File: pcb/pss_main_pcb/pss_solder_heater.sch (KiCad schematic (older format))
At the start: 43 parts

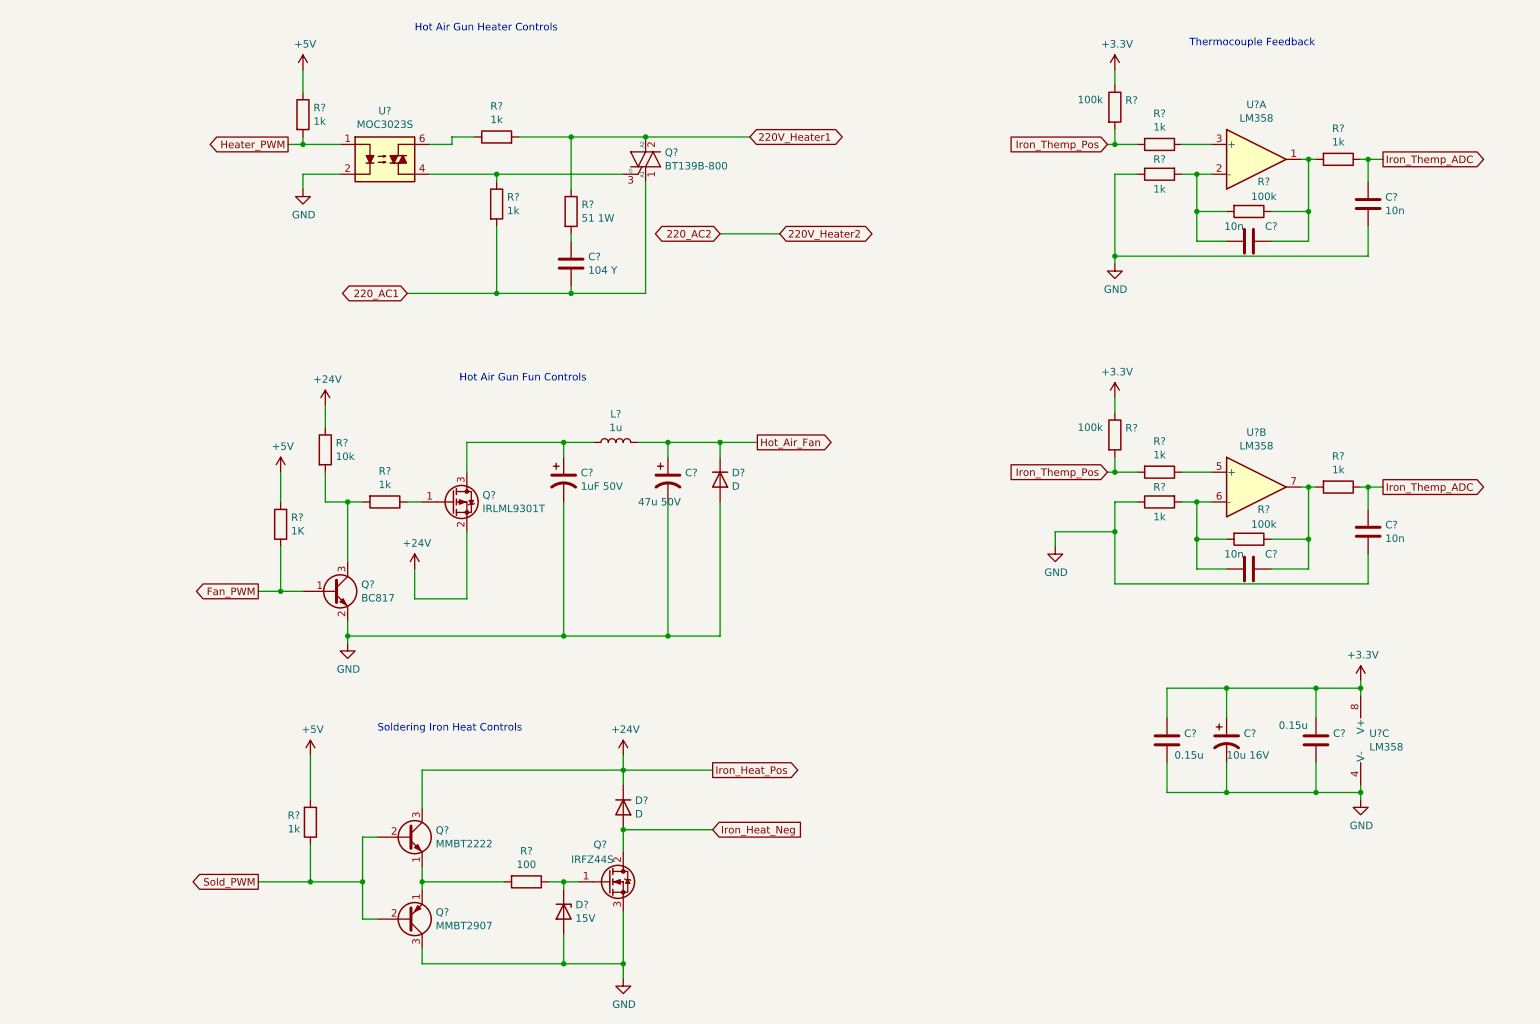
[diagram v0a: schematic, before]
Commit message: Add stm32 schematics
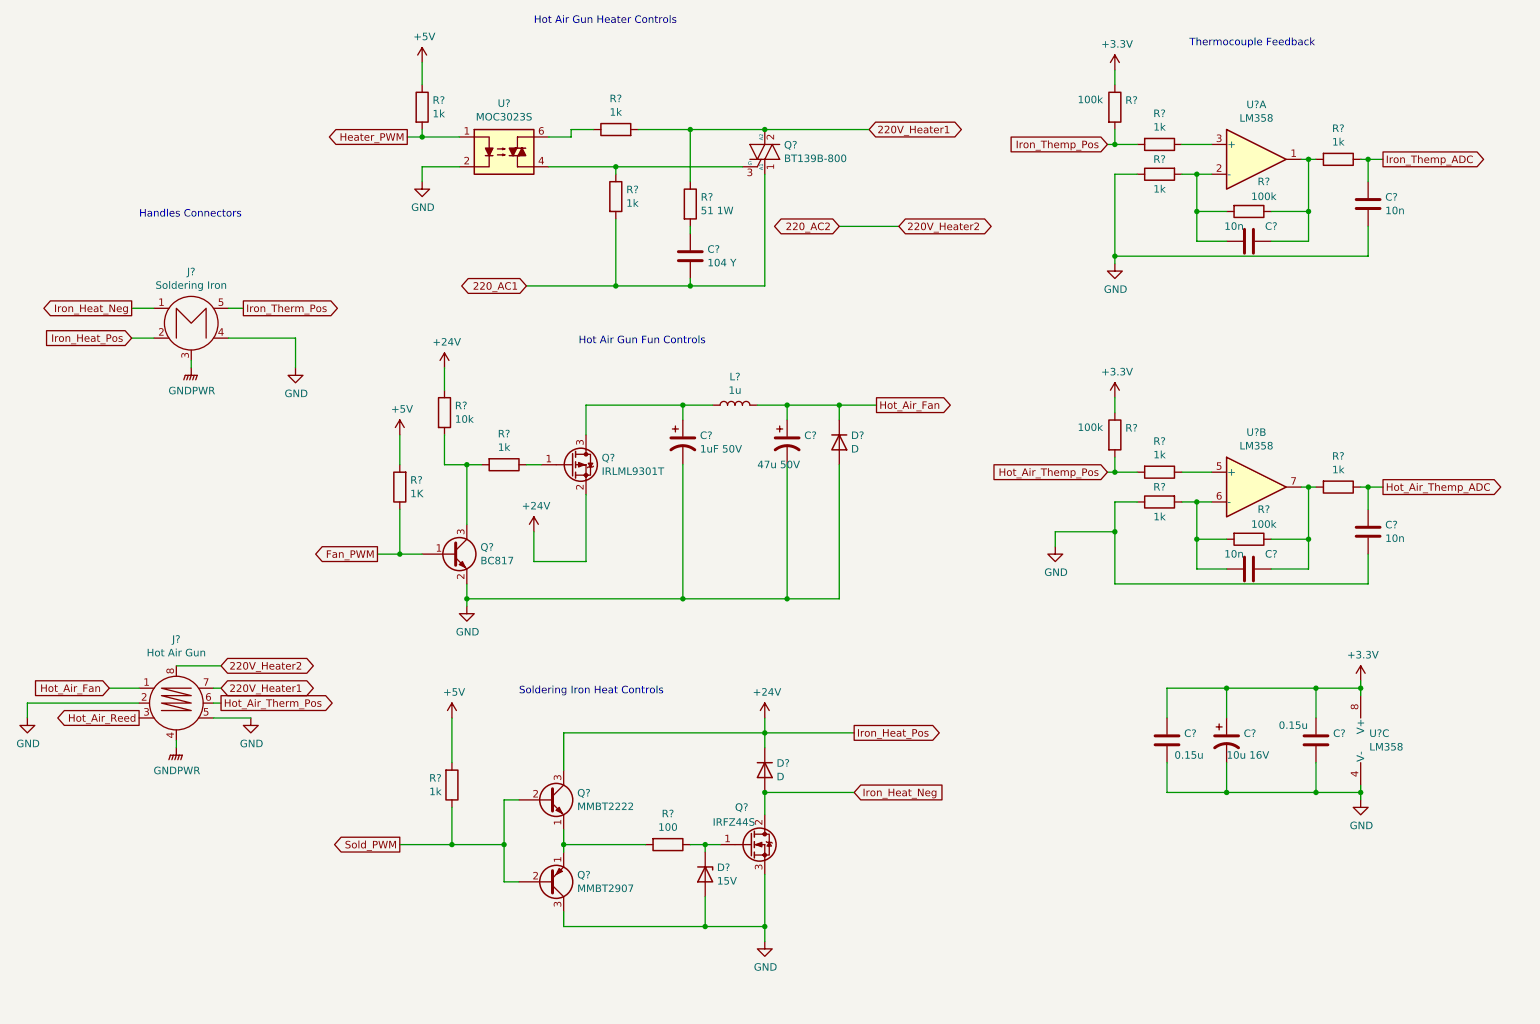
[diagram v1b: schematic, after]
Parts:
- added J?: Soldering Iron, symbol gx16_conn:GX16-M5_connector
- added J?: Hot Air Gun, symbol gx16_conn:GX16-M8_connector
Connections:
- net +24V: now also J?.2
- net 220V_Heater1: now also J?.7
- net 220V_Heater2: now also J?.8
- net GND: now also J?.2, J?.4, J?.5
- net Hot_Air_Fan: now also J?.1
- net Iron_Heat_Neg: now also J?.1
- net Iron_Themp_ADC: no longer C?.1, R?.1
- net Iron_Themp_Pos: no longer R?.2, R?.2
- new net GNDPWR: J?.3, J?.4
- new net Hot_Air_Reed: J?.3
- new net Hot_Air_Themp_ADC: C?.1, R?.1
- new net Hot_Air_Themp_Pos: R?.2, R?.2
- new net Hot_Air_Therm_Pos: J?.6
- new net Iron_Therm_Pos: J?.5
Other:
- note added: "Handles Connectors\n"
- moved on the sheet: C?, D?, L?, Q?, R?, U?

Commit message: Fix schematics
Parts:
- gave numbers to parts that had none: 43
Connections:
- net Hot_Air_Themp_Pos is gone; now on net Hot_Air_Therm_Pos: R12.2, R15.2
- net Iron_Themp_Pos is gone; now on net Iron_Therm_Pos: R11.2, R13.2

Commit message: Add footprints for AC controls components
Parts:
- J3: footprint (none) -> gx_connectors:GX16-8
- U3: footprint (none) -> moc3023s:SOT254P1016X460-6N
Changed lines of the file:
@@
-$EndComp
-$Comp
-L Opto_custom:MOC3023S U?
-U 1 1 5EE25046
-P 3950 1700
-AR Path="/5EE25046" Ref="U?"  Part="1"
-AR Path="/5EE1CBE0/5EE25046" Ref="U3"  Part="1"
-F 0 "U3" H 3950 2025 50  0000 C CNN
-F 1 "MOC3023S" H 3950 1934 50  0000 C CNN
-F 2 "" H 3750 1500 50  0001 L CIN
-F 3 "https://optoelectronics.liteon.com/upload/download/DS-70-99-0019/MOC302X%20series%20201606.pdf" H 3925 1700 50  0001 L CNN
-	1    3950 1700
-	1    0    0    -1
-$EndComp
-$Comp
-L Triac_custom:BT139B-800 Q?
-U 1 1 5EE2504D
-P 5700 1700
-AR Path="/5EE2504D" Ref="Q?"  Part="1"
-AR Path="/5EE1CBE0/5EE2504D" Ref="Q6"  Part="1"
-F 0 "Q6" H 5829 1746 50  0000 L CNN
-F 1 "BT139B-800" H 5829 1655 50  0000 L CNN
-F 2 "Package_TO_SOT_THT:SOT-404" H 5900 1625 50  0001 L CIN
-F 3 "https://www.ariat-tech.com/datasheet/42/SBR545D1-13.pdf" H 5700 1700 50  0001 L CNN
-	1    5700 1700
-	1    0    0    -1
 $EndComp
 $Comp
@@
 F 0 "J3" H 1750 5828 50  0000 C CNN
 F 1 "Hot Air Gun" H 1750 5737 50  0000 C CNN
-F 2 "" H 1750 5400 50  0001 C CNN
+F 2 "gx_connectors:GX16-8" H 1750 5400 50  0001 C CNN
 F 3 "" H 1750 5400 50  0001 C CNN
 	1    1750 5400
@@
 Wire Wire Line
 	1200 6950 1200 6750
+$Comp
+L Triac_custom:BT139B-800 Q?
+U 1 1 5EE2504D
+P 5700 1700
+AR Path="/5EE2504D" Ref="Q?"  Part="1"
+AR Path="/5EE1CBE0/5EE2504D" Ref="Q6"  Part="1"
+F 0 "Q6" H 5829 1746 50  0000 L CNN
+F 1 "BT139B-800" H 5829 1655 50  0000 L CNN
+F 2 "Package_TO_SOT_THT:SOT-404" H 5900 1625 50  0001 L CIN
+F 3 "https://www.ariat-tech.com/datasheet/42/SBR545D1-13.pdf" H 5700 1700 50  0001 L CNN
+	1    5700 1700
+	1    0    0    -1
+$EndComp
+$Comp
+L Opto_custom:MOC3023S U?
+U 1 1 5EE25046
+P 3950 1700
+AR Path="/5EE25046" Ref="U?"  Part="1"
+AR Path="/5EE1CBE0/5EE25046" Ref="U3"  Part="1"
+F 0 "U3" H 3950 2025 50  0000 C CNN
+F 1 "MOC3023S" H 3950 1934 50  0000 C CNN
+F 2 "moc3023s:SOT254P1016X460-6N" H 3750 1500 50  0001 L CIN
+F 3 "https://optoelectronics.liteon.com/upload/download/DS-70-99-0019/MOC302X%20series%20201606.pdf" H 3925 1700 50  0001 L CNN
+	1    3950 1700
+	1    0    0    -1
+$EndComp
 $EndSCHEMATC

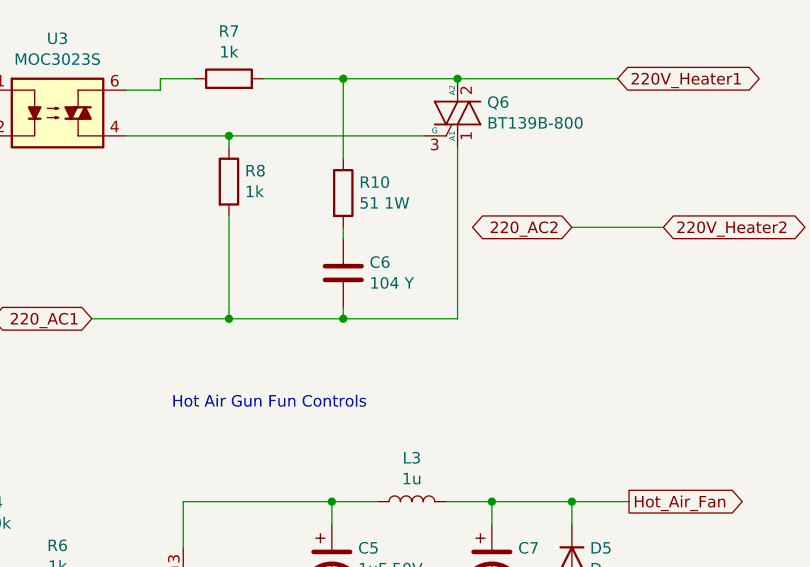
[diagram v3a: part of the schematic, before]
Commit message: Change safety capacitor footprint
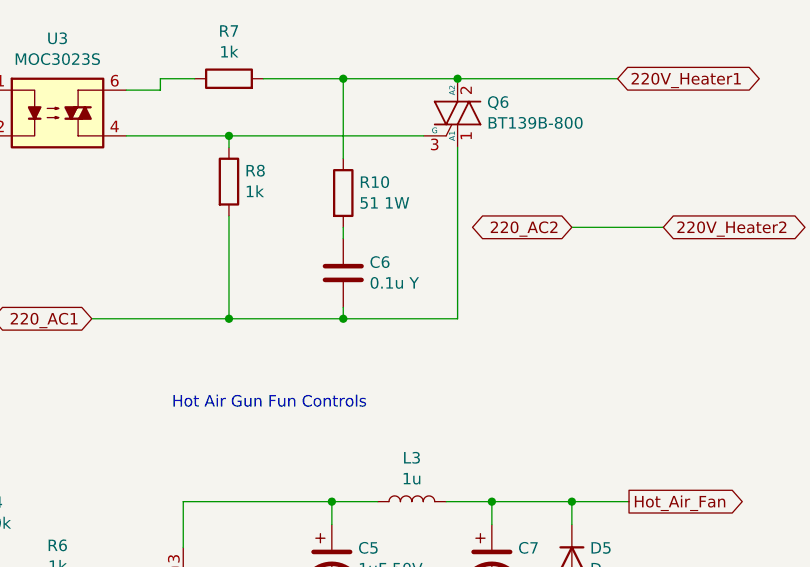
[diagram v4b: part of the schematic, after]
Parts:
- C6: value 104 Y -> 0.1u Y; footprint (none) -> Capacitor_THT:C_Rect_L10.0mm_W2.5mm_P7.50mm_MKS4
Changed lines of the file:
@@
 AR Path="/5EE1CBE0/5EE25071" Ref="C6"  Part="1"
 F 0 "C6" H 5315 2446 50  0000 L CNN
-F 1 "104 Y" H 5315 2355 50  0000 L CNN
-F 2 "" H 5238 2250 50  0001 C CNN
+F 1 "0.1u Y" H 5315 2355 50  0000 L CNN
+F 2 "Capacitor_THT:C_Rect_L10.0mm_W2.5mm_P7.50mm_MKS4" H 5238 2250 50  0001 C CNN
 F 3 "~" H 5200 2400 50  0001 C CNN
 	1    5200 2400

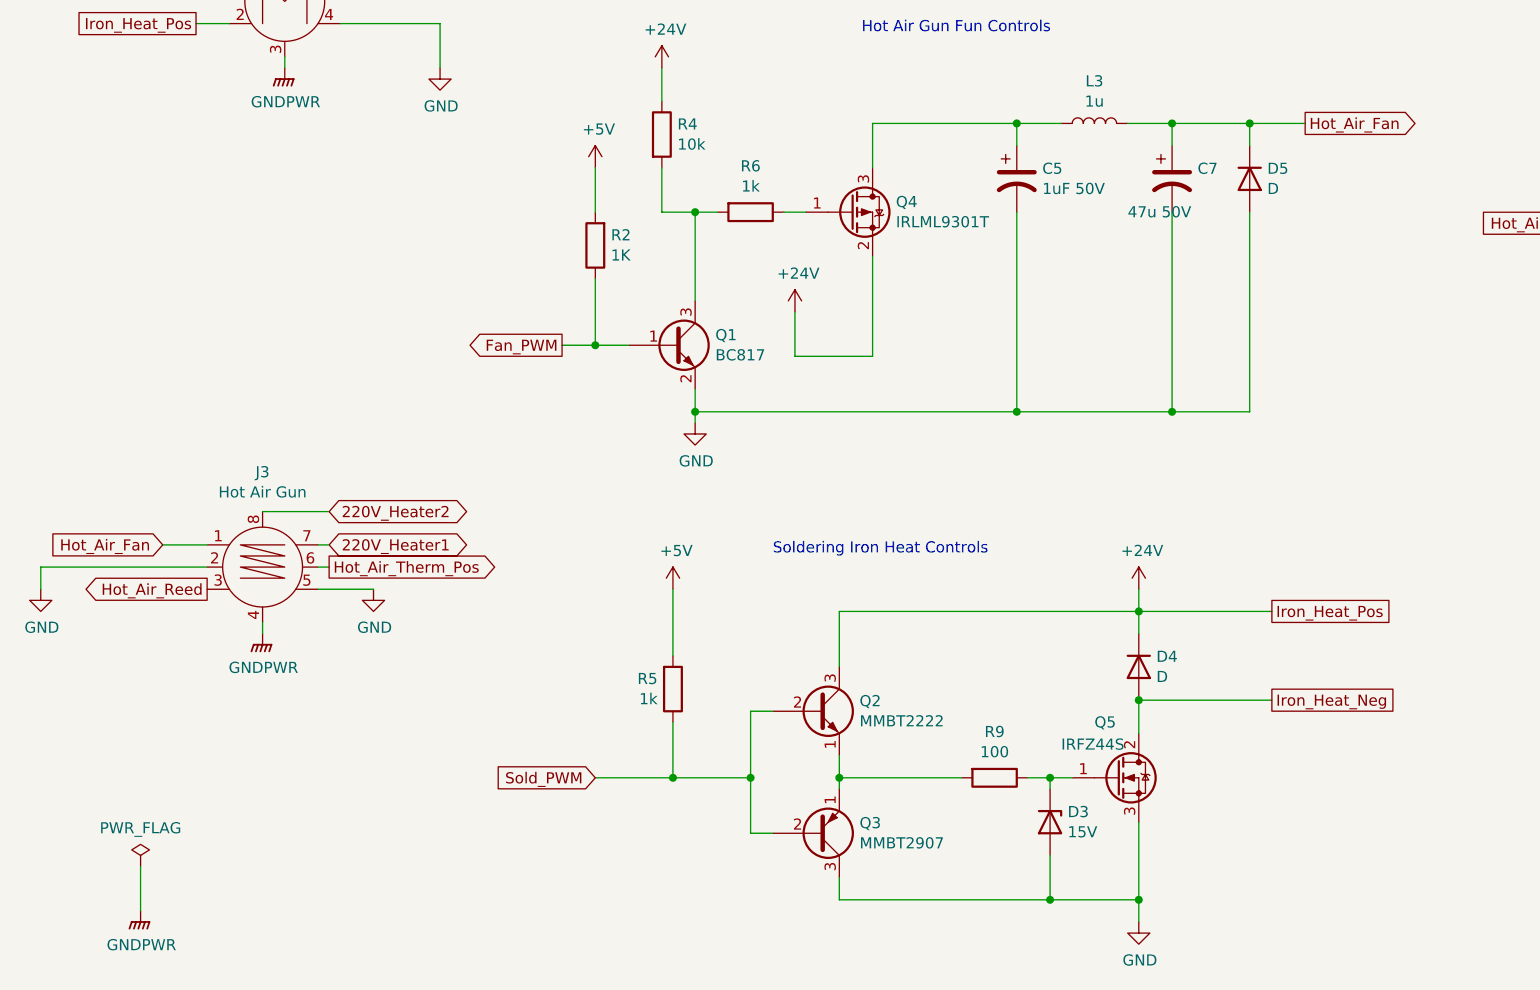
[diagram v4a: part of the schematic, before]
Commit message: Add footprints for heaters controls
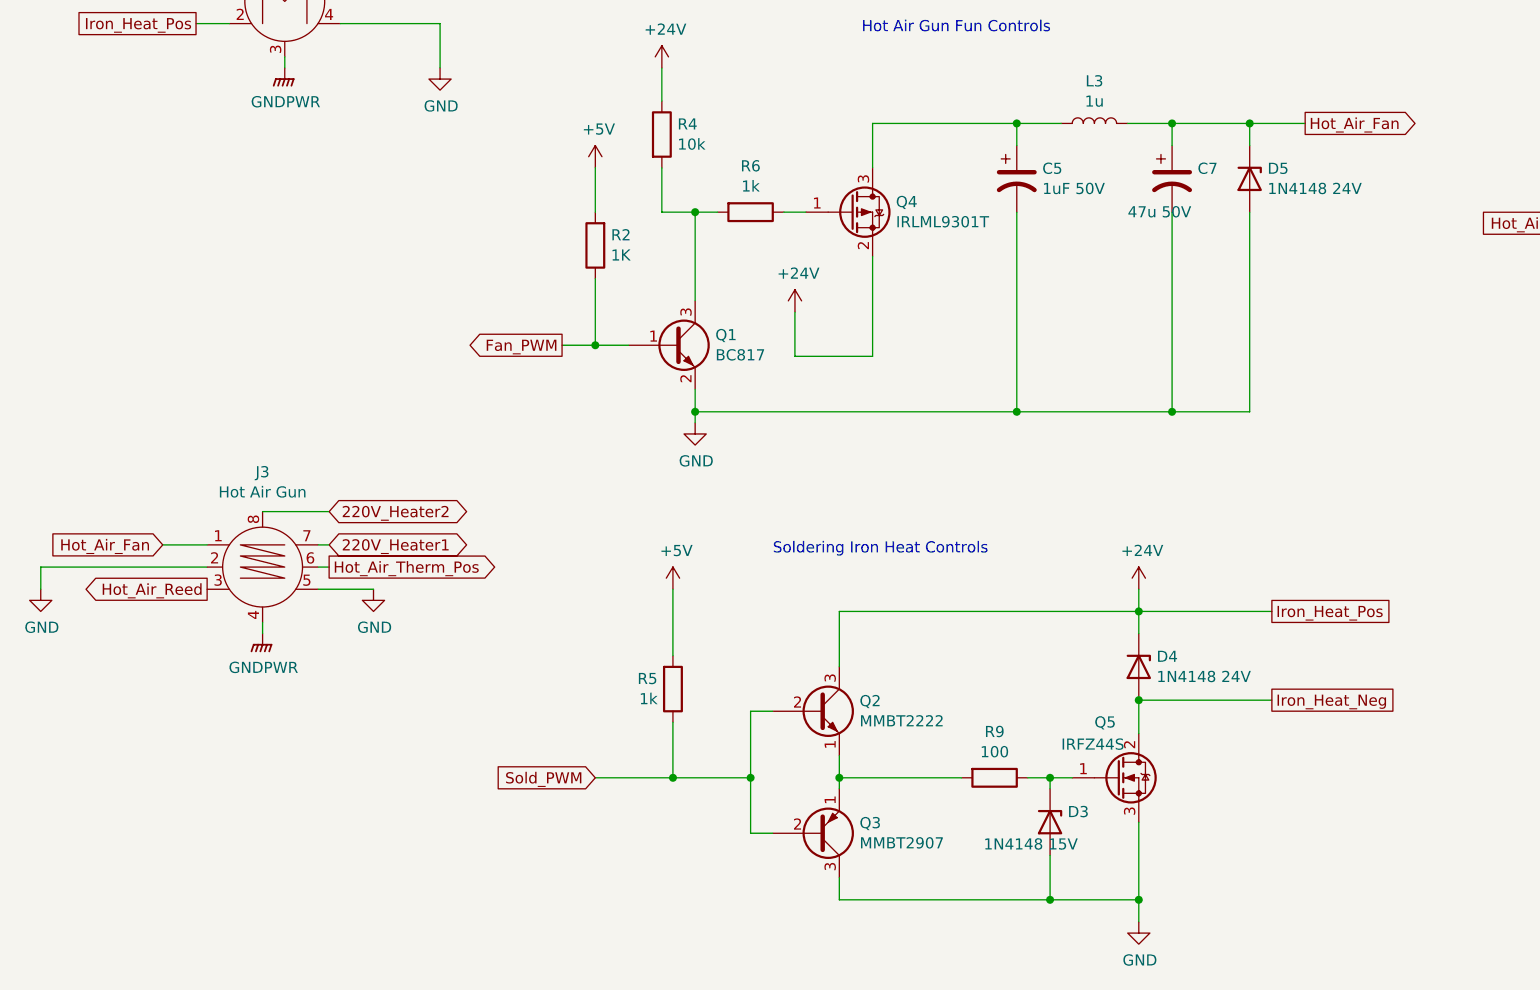
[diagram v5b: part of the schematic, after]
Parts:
- removed D4, D5: D, symbol Device:D
- added D4, D5: 1N4148 24V, Diode_SMD:D_1206_3216Metric_Pad1.42x1.75mm_HandSolder, symbol Device:D_Zener
- C10, C11, C12, C13, C14, C8: footprint (none) -> Capacitor_SMD:C_1206_3216Metric_Pad1.42x1.75mm_HandSolder
- C5, C7: footprint (none) -> Capacitor_SMD:CP_Elec_16x17.5
- C9: footprint (none) -> Capacitor_SMD:CP_Elec_8x10.5
- D3: value 15V -> 1N4148 15V; footprint (none) -> Diode_SMD:D_1206_3216Metric_Pad1.42x1.75mm_HandSolder
- L3: footprint (none) -> Inductor_SMD:L_Wuerth_HCI-1030
- Q1, Q4: footprint Package_TO_SOT_SMD:SOT-23 -> Package_TO_SOT_SMD:SOT-23_Handsoldering
- Q2, Q3: footprint Package_TO_SOT_THT:TO-92_Inline -> Package_TO_SOT_SMD:SOT-23_Handsoldering
- R10, R11, R12, R13, R14, R15, R16, R17, R18, R19, R2, R20, R3, R4, R5, R6, R7, R8, R9: footprint (none) -> Resistor_SMD:R_1206_3216Metric_Pad1.42x1.75mm_HandSolder
- U4: footprint (none) -> Package_SO:SOIC-8_3.9x4.9mm_P1.27mm
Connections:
- net +24V: now also D4.1 (K)
- net GND: now also D5.2 (A)
- net Hot_Air_Fan: now also D5.1 (K)
- net Iron_Heat_Neg: now also D4.2 (A)

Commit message: Add footprints
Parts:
- J4: footprint (none) -> gx_connectors:GX16-5
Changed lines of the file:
@@
 F 0 "J4" H 1850 3195 50  0000 C CNN
 F 1 "Soldering Iron" H 1850 3104 50  0000 C CNN
-F 2 "" H 2500 2900 50  0001 C CNN
+F 2 "gx_connectors:GX16-5" H 2500 2900 50  0001 C CNN
 F 3 "" H 2500 2900 50  0001 C CNN
 	1    1850 2850

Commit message: Create netlist and place some components
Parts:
- Q6: footprint Package_TO_SOT_THT:SOT-404 -> bt139b:D2PAK-3
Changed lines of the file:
@@
 F 0 "Q6" H 5829 1746 50  0000 L CNN
 F 1 "BT139B-800" H 5829 1655 50  0000 L CNN
-F 2 "Package_TO_SOT_THT:SOT-404" H 5900 1625 50  0001 L CIN
+F 2 "bt139b:D2PAK-3" H 5900 1625 50  0001 L CIN
 F 3 "https://www.ariat-tech.com/datasheet/42/SBR545D1-13.pdf" H 5700 1700 50  0001 L CNN
 	1    5700 1700
